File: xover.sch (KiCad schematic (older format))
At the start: 23 parts, among them J1 Conn_01x03_Male, J2 Screw_Terminal_01x04, J3 Screw_Terminal_01x02, J4 Conn_02x03_Odd_Even, J5 Screw_Terminal_01x04, J6 Screw_Terminal_01x04, U1 NE5532

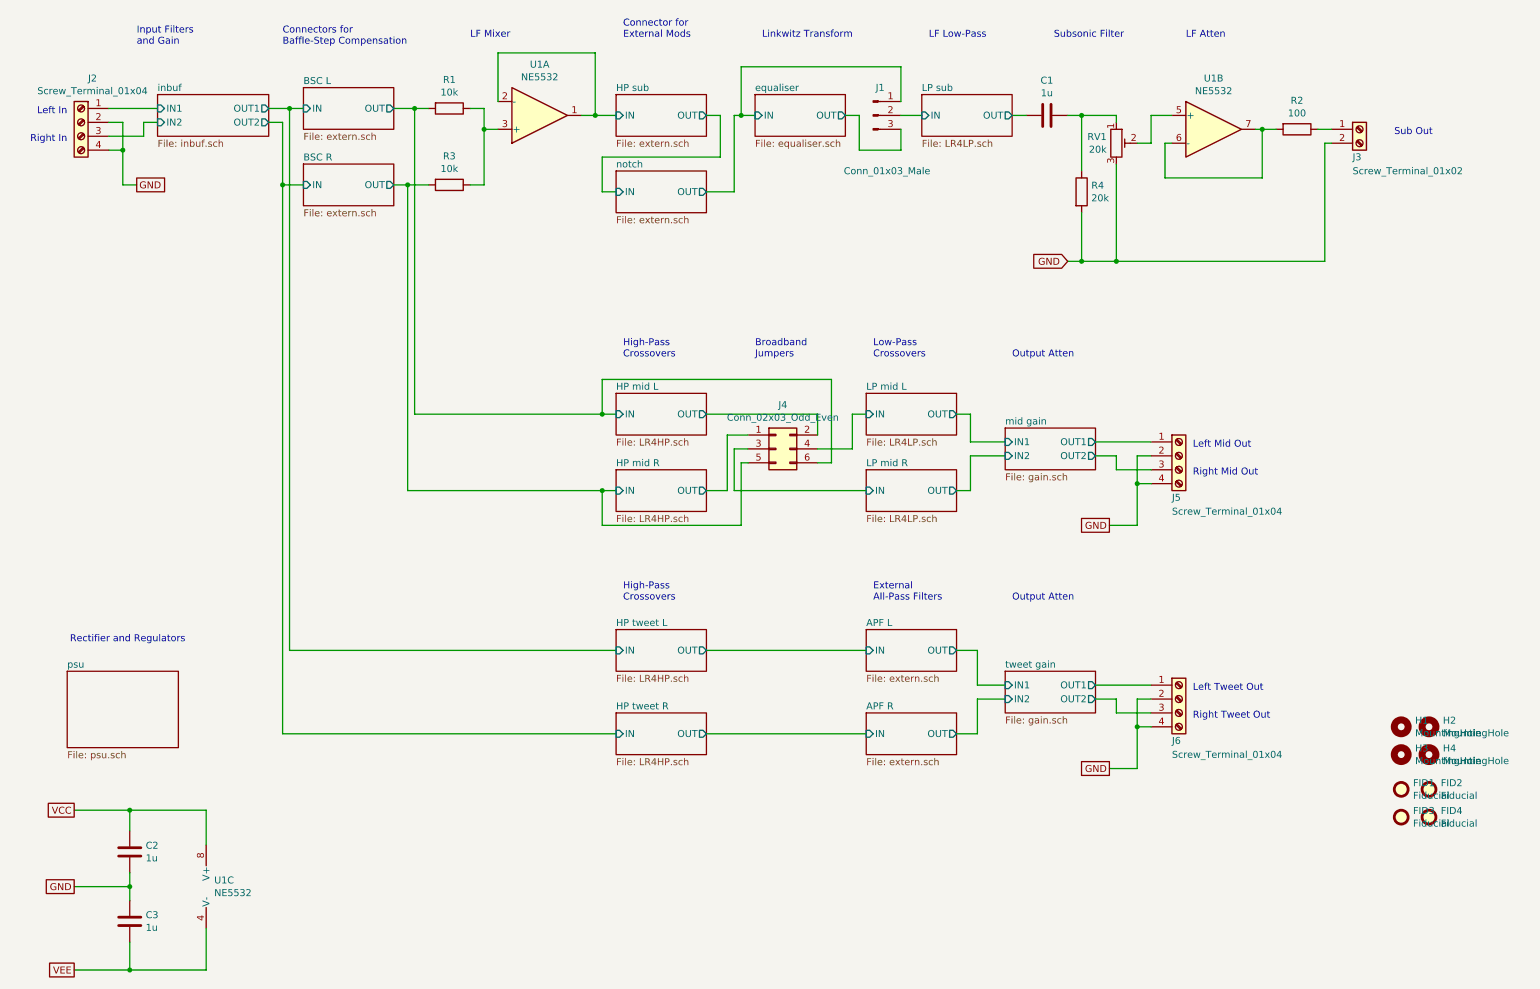
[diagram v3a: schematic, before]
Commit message: inverted LF processing chain, now with BW2 subsonic filter
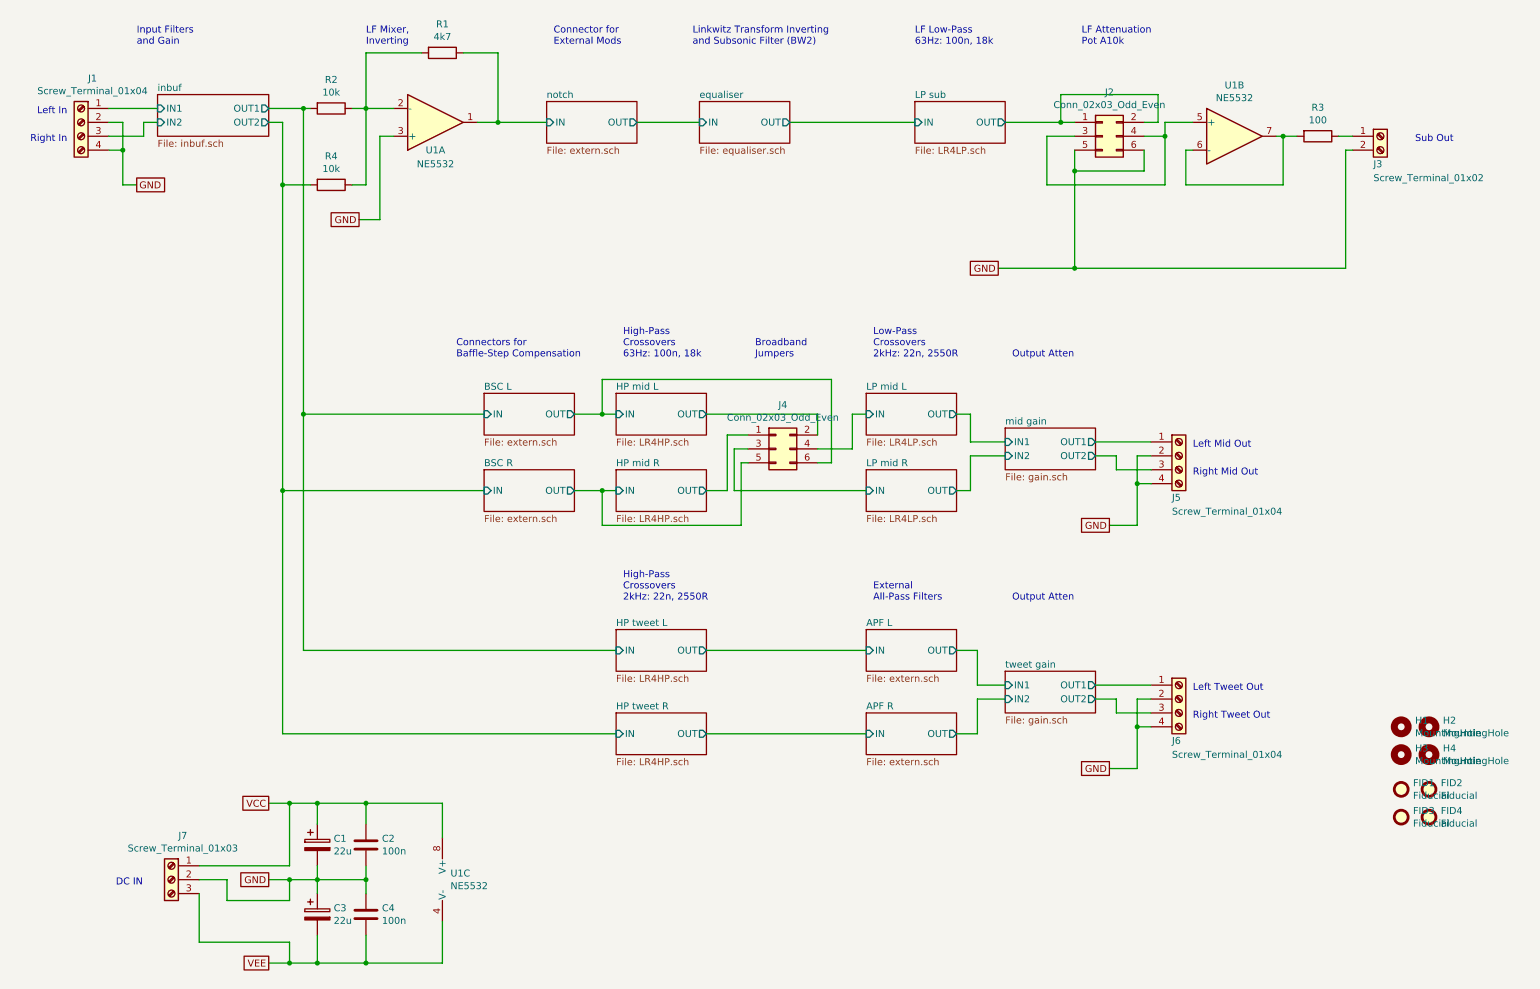
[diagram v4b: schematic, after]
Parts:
- removed C1: 1u, Capacitors_ThroughHole:C_Rect_L7.2mm_W7.2mm_P5.00mm_FKS2_FKP2_MKS2_MKP2, symbol Device:C
- removed J1: Conn_01x03_Male, Pin_Headers:Pin_Header_Straight_1x03_Pitch2.54mm, symbol Connector:Conn_01x03_Male
- removed R4: 20k, Resistors_SMD:R_0805, symbol Device:R
- removed RV1: 20k, Potentiometers:Potentiometer_Trimmer_Bourns_3296W, symbol Device:R_POT_TRIM
- added C1, C3: 22u, Capacitors_ThroughHole:CP_Radial_Tantal_D5.0mm_P5.00mm, symbol Device:CP
- added J2: Conn_02x03_Odd_Even, Pin_Headers:Pin_Header_Straight_2x03_Pitch2.54mm, symbol Connector_Generic:Conn_02x03_Odd_Even
- added J7: Screw_Terminal_01x03, Terminals_Phoenix:TerminalBlock_Phoenix_MKDS1.5-3pol, symbol Connector:Screw_Terminal_01x03
- added R1: 4k7, Resistors_SMD:R_0805, symbol Device:R
- C2: value 1u -> 100n
- C4: renamed from C3; value 1u -> 100n
- renumbered J2 to J1, R1 to R2, R2 to R3, R3 to R4
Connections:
- net BSC L/IN: now also R2.2
- net BSC L/OUT: no longer R2.2
- net BSC R/IN: now also R4.2
- net BSC R/OUT: no longer R4.2
- net GND: now also U1.3 (+), C1.2, C3.1, J2.5 (Pin_5), J2.6 (Pin_6), J7.2 (Pin_2)
- net LP sub/OUT: now also J2.1 (Pin_1), J2.2 (Pin_2)
- net VCC: now also C1.1, J7.1 (Pin_1)
- net VEE: now also C3.2, J7.3 (Pin_3)
- net at R2.1, R4.1: now also U1.2 (-), R1.2; no longer U1.3 (+)
- net at U1.5 (+): now also J2.3 (Pin_3), J2.4 (Pin_4)
- net HP sub/IN renamed notch/IN
- net notch/IN: now also R1.1; no longer U1.2 (-)
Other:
- note added: "DC IN"
- note added: "High-Pass\nCrossovers\n2kHz: 22n, 2550R"
- note added: "High-Pass\nCrossovers\n63Hz: 100n, 18k"
- note added: "LF Attenuation\nPot A10k"
- note added: "LF Low-Pass\n63Hz: 100n, 18k"
- note added: "LF Mixer,\nInverting"
- note added: "Linkwitz Transform Inverting\nand Subsonic Filter (BW2)"
- note added: "Low-Pass\nCrossovers\n2kHz: 22n, 2550R"
- note removed: "High-Pass\nCrossovers"
- note removed: "LF Atten"
- note removed: "LF Low-Pass"
- note removed: "LF Mixer"
- note removed: "Linkwitz Transform"
- note removed: "Low-Pass\nCrossovers"
- note removed: "Rectifier and Regulators"
- note removed: "Subsonic Filter"
- moved on the sheet: C2, C4, J3, R2, R3, R4, U1A, U1B, U1C

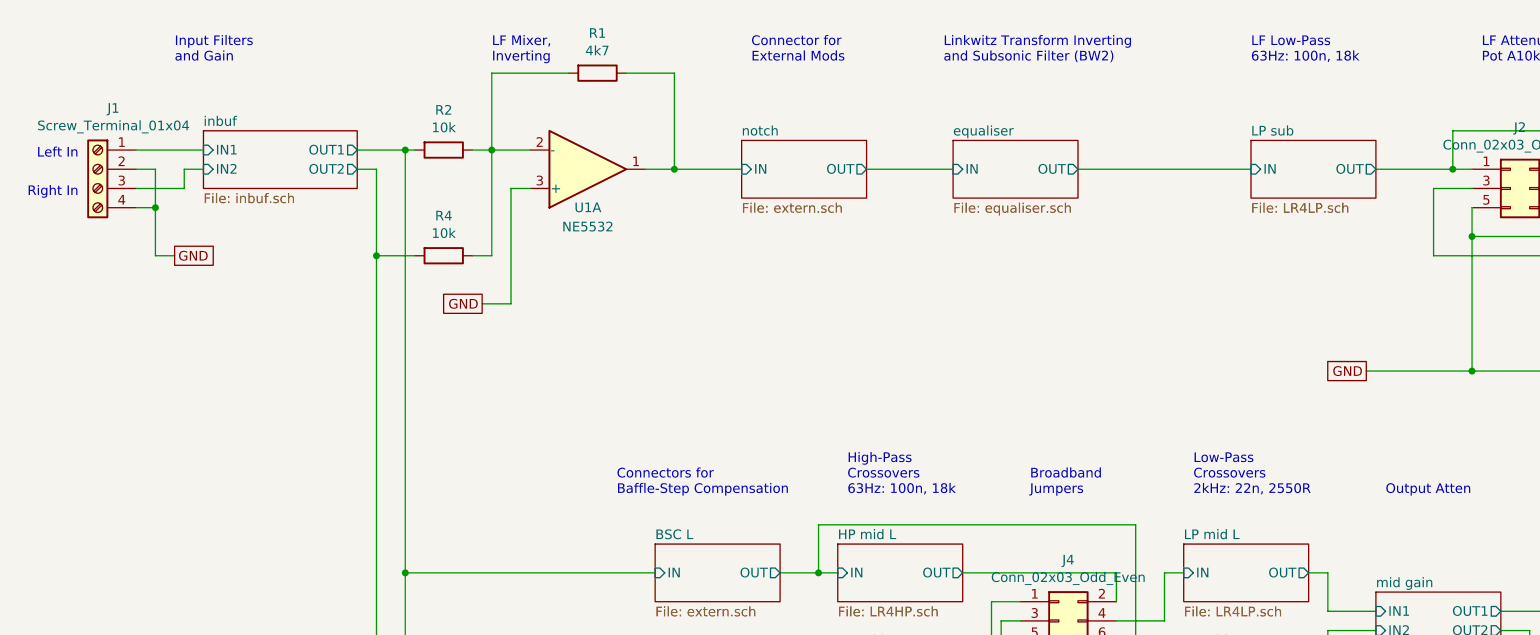
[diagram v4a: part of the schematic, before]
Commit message: Rev.B adds "hum break resistor" in input network
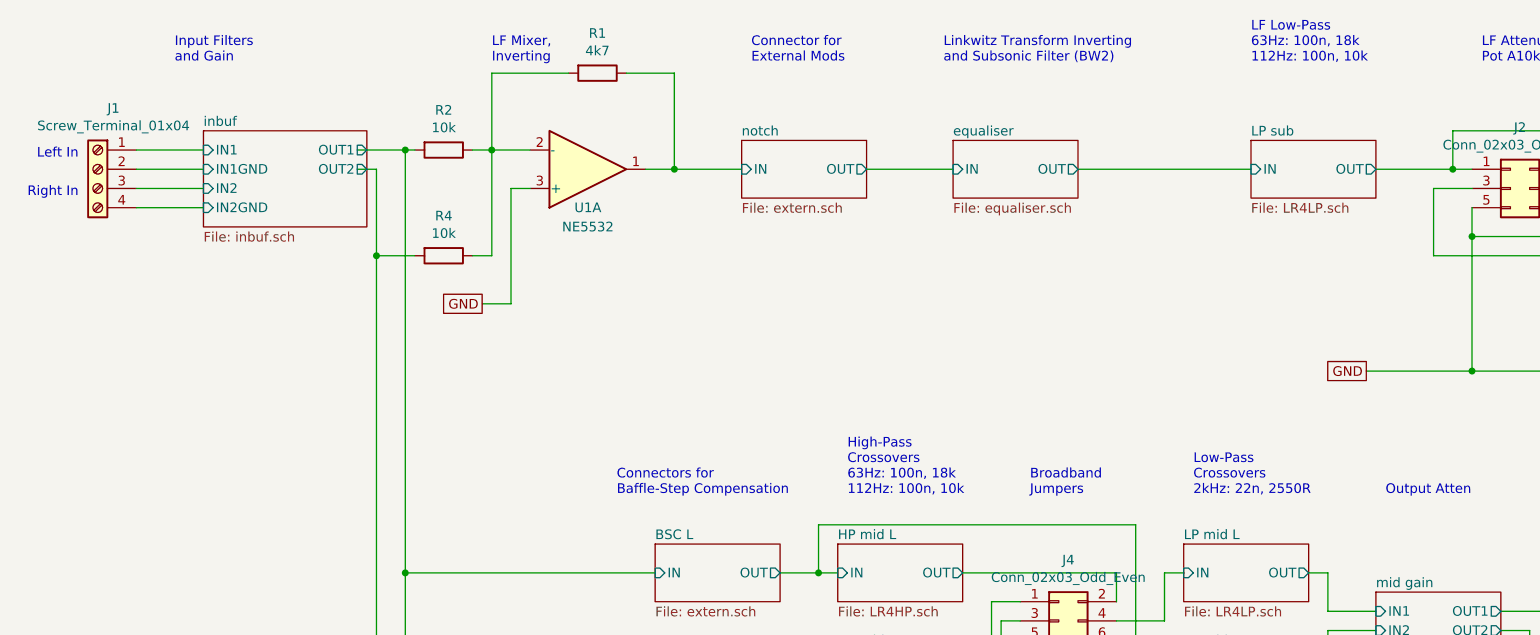
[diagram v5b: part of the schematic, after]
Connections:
- net GND: no longer J1.2 (Pin_2), J1.4 (Pin_4)
- new net inbuf/IN1GND: J1.2 (Pin_2)
- new net inbuf/IN2GND: J1.4 (Pin_4)
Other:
- note added: "High-Pass\nCrossovers\n63Hz: 100n, 18k\n112Hz: 100n, 10k"
- note added: "LF Low-Pass\n63Hz: 100n, 18k\n112Hz: 100n, 10k"
- note removed: "High-Pass\nCrossovers\n63Hz: 100n, 18k"
- note removed: "LF Low-Pass\n63Hz: 100n, 18k"
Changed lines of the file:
@@
 Sheet 1 17
 Title "Active Crossovers for 2x2.1 Speakers"
-Date "2021-10-03"
-Rev "A"
+Date "2022-01-12"
+Rev "B"
 Comp "Tyrrell Zaibatsu"
 Comment1 ""
@@
 $EndSheet
 $Sheet
-S 1500 1200 800  300
+S 1500 1200 850  500
 U 6159A74A
 F0 "inbuf" 50
 F1 "inbuf.sch" 50
 F2 "IN1" I L 1500 1300 50
-F3 "IN2" I L 1500 1400 50
-F4 "OUT1" O R 2300 1300 50
-F5 "OUT2" O R 2300 1400 50
+F3 "IN2" I L 1500 1500 50
+F4 "OUT1" O R 2350 1300 50
+F5 "OUT2" O R 2350 1400 50
+F6 "IN1GND" I L 1500 1400 50
+F7 "IN2GND" I L 1500 1600 50
 $EndSheet
 $Sheet
@@
 Wire Wire Line
 	1150 1300 1500 1300
-Wire Wire Line
-	1150 1500 1400 1500
-Wire Wire Line
-	1400 1500 1400 1400
-Wire Wire Line
-	1400 1400 1500 1400
-Text GLabel 1350 1850 2    50   UnSpc ~ 0
-GND
-Wire Wire Line
-	1150 1400 1250 1400
-Wire Wire Line
-	1250 1400 1250 1600
-Wire Wire Line
-	1250 1850 1350 1850
 $Comp
 L Connector:Screw_Terminal_01x04 J1
@@
 	-1   0    0    -1
 $EndComp
-Wire Wire Line
-	1150 1600 1250 1600
-Connection ~ 1250 1600
-Wire Wire Line
-	1250 1600 1250 1850
 Text GLabel 8350 4300 0    50   UnSpc ~ 0
 GND
@@
 LF Mixer,\nInverting
 Text Notes 6950 850  0    50   ~ 0
-LF Low-Pass\n63Hz: 100n, 18k
+LF Low-Pass\n63Hz: 100n, 18k\n112Hz: 100n, 10k
 Text Notes 5350 850  0    50   ~ 0
 Linkwitz Transform Inverting\nand Subsonic Filter (BW2)
@@
 	4800 5800 2400 5800
 Text Notes 4850 3100 0    50   ~ 0
-High-Pass\nCrossovers\n63Hz: 100n, 18k
+High-Pass\nCrossovers\n63Hz: 100n, 18k\n112Hz: 100n, 10k
 Text Notes 6650 3100 0    50   ~ 0
 Low-Pass\nCrossovers\n2kHz: 22n, 2550R
@@
 Wire Wire Line
 	3200 1500 3100 1500
+Wire Wire Line
+	1150 1400 1500 1400
+Wire Wire Line
+	1150 1500 1500 1500
+Wire Wire Line
+	1150 1600 1500 1600
 $EndSCHEMATC
